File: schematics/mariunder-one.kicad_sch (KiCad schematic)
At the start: 44 parts, among them J1 Conn_01x07_I2S, J2 USB_A, J3 Conn_01x02, J4 Conn_02x04_C1101, Q1 2N3904, SW1 SW_Push_Dual_UP, SW10 SW_Push_Dual_BTN_A, SW11 SW_SPDT, SW2 SW_Push_Dual_DOWN, SW3 SW_Push_Dual_LEFT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

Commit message: updated project structure
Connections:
- net VBAT: now also J3.2 (Pin_2), tp1.6 (B-)
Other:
- moved on the sheet: C2, C3, C4, D2, H1, H2, H3, H4, J1, J2, J3, J4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

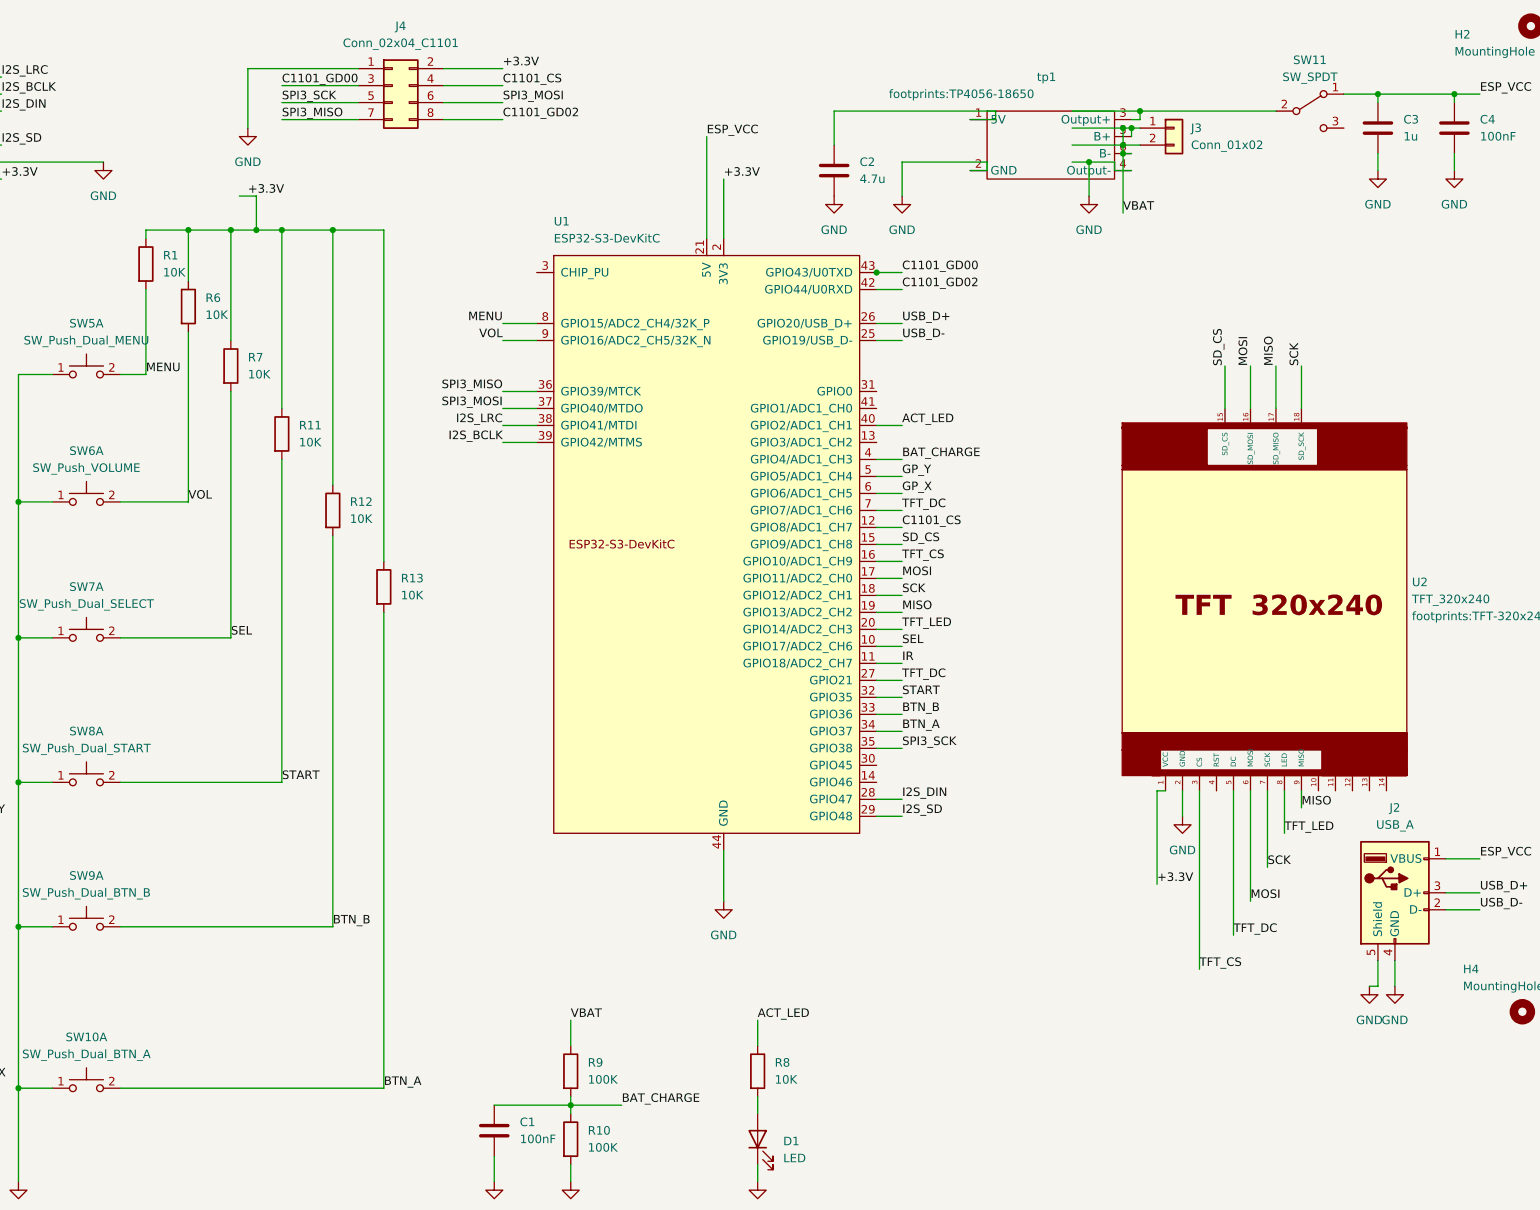
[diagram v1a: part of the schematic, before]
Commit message: Switched btn a,b, select and start to ADC2 as GPIO 35,36 and 37 are used in octal PSRAM mode
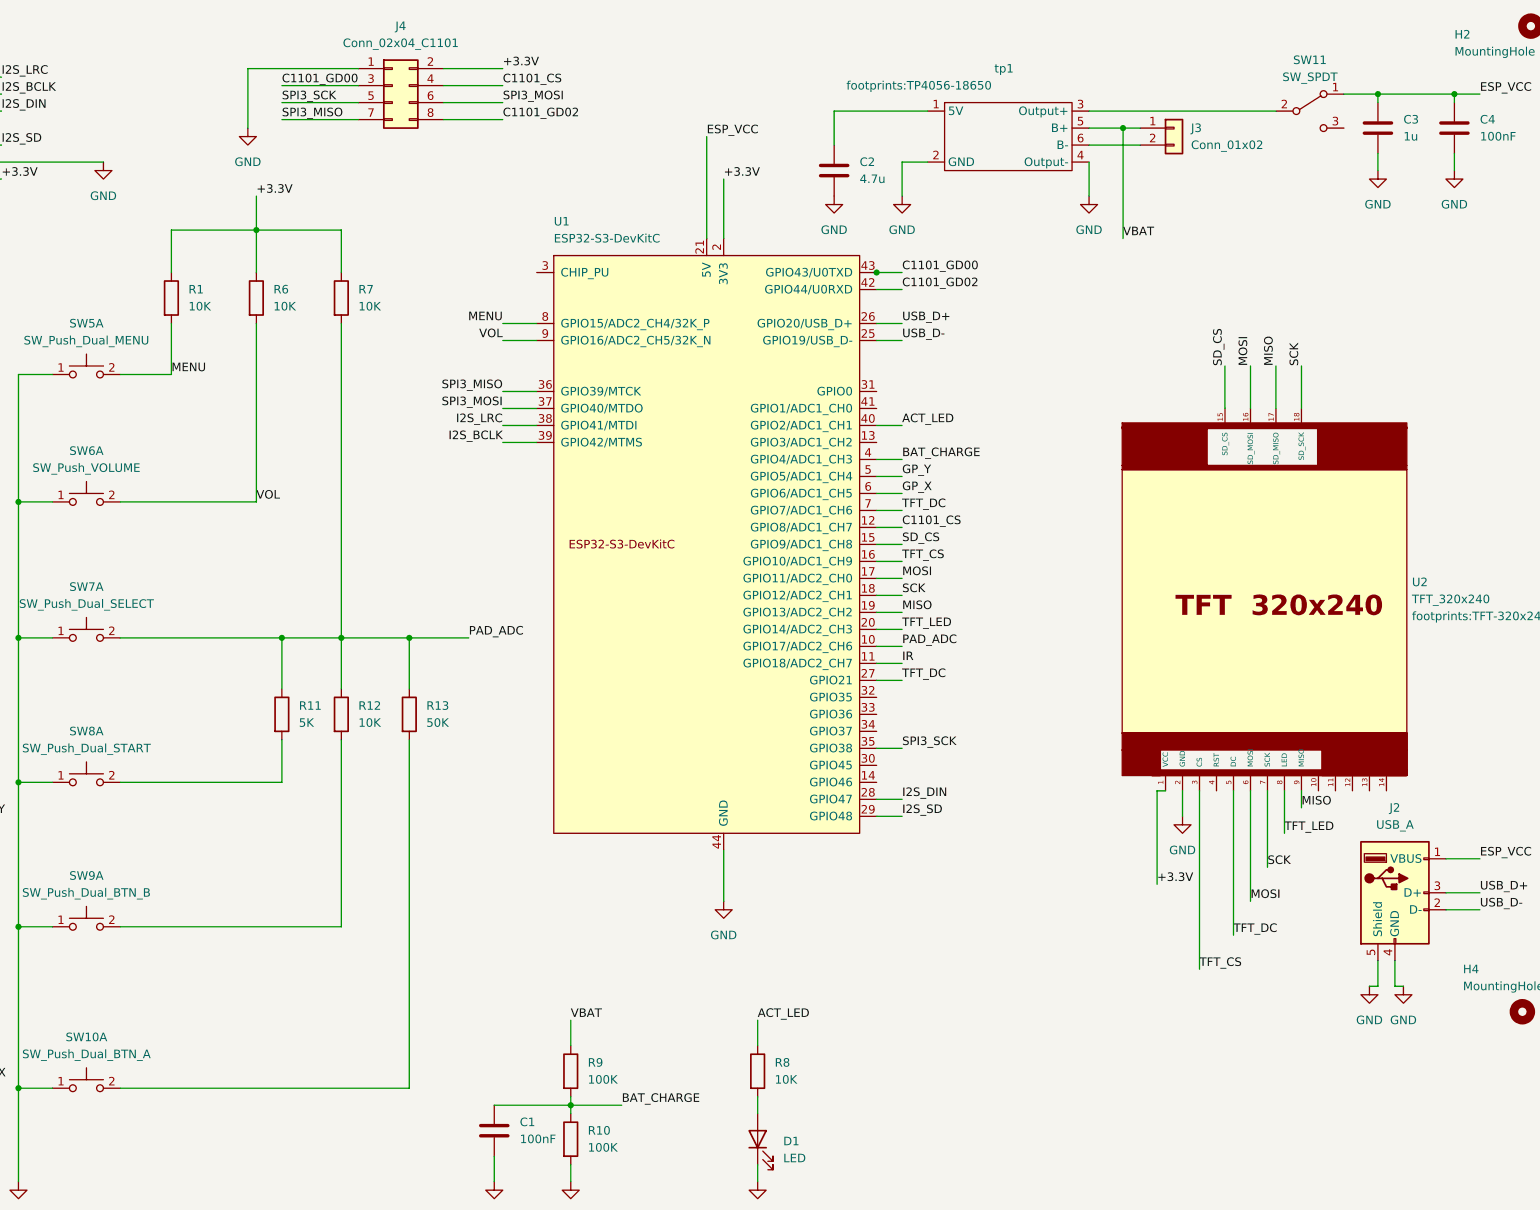
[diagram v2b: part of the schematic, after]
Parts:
- R11: value 10K -> 5K
- R13: value 10K -> 50K
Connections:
- net +3.3V: no longer R11.1, R12.1, R13.1
- net VBAT: no longer J3.2 (Pin_2), tp1.6 (B-)
- net BTN_A: no longer names the net of R13.2, SW10.2 (D)
- net BTN_A: no longer U1.34 (GPIO37)
- net BTN_B: no longer names the net of R12.2, SW9.2 (D)
- net BTN_B: no longer U1.33 (GPIO36)
- net SEL renamed PAD_ADC
- net PAD_ADC: now also R11.1, R12.1, R13.1
- net START: no longer names the net of R11.2, SW8.2 (D)
- net START: no longer U1.32 (GPIO35)
- new net: J3.2 (Pin_2), tp1.6 (B-)
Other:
- moved on the sheet: R1, R11, R12, R13, R6, R7, tp1
